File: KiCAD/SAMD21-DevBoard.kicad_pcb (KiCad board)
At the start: 2 copper layers, 28 x 60 mm, 34 parts, among them J1 .1" Headers, J2 .1" Headers, J3 Cortex_Debug, J4 USB-Micro, Q1 3.7A, 30V, SW1 B3FS-4005P, U1 SAMD21G18A-AU, U2 LM1117-5.0, U3 AP2112K-3.3, Y1 32.768KHz

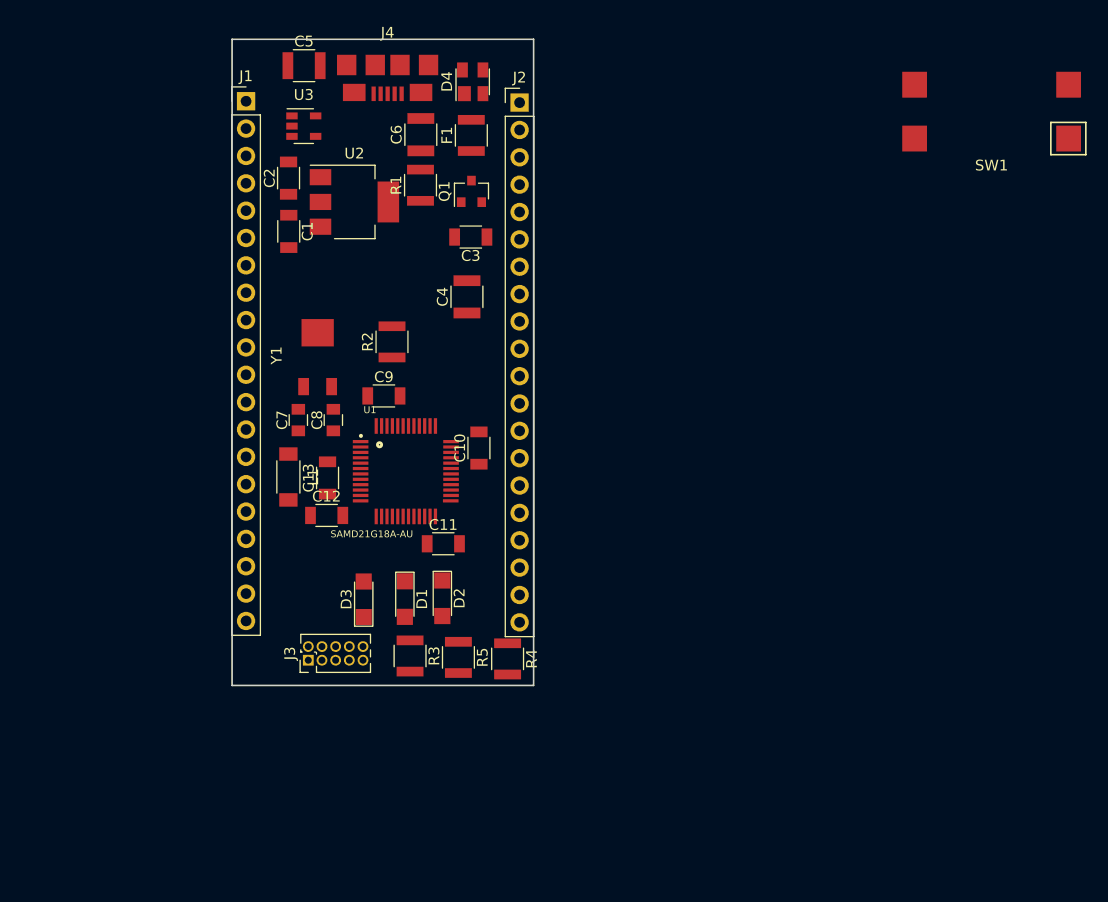
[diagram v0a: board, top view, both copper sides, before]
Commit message: Board layout and fixing schematic errors
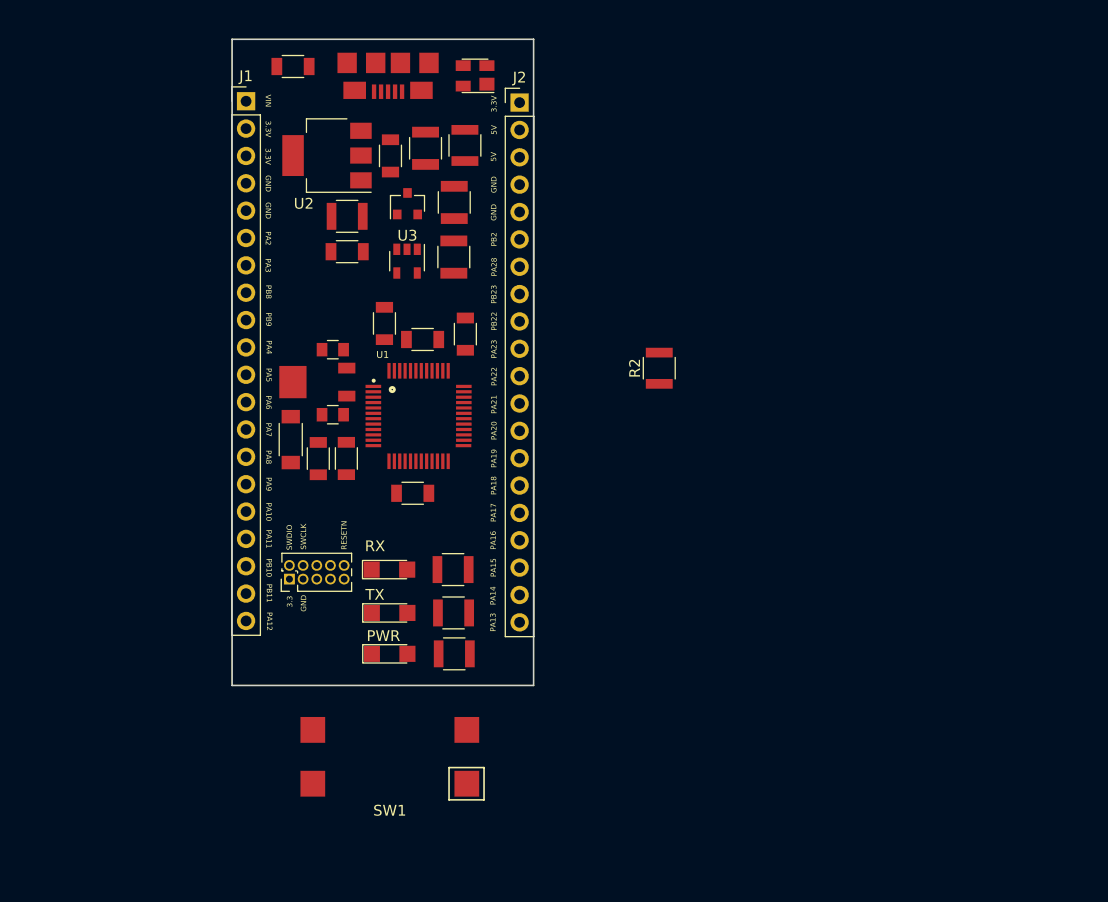
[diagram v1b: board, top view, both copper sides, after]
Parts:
- added C14: .1uF, Capacitors_SMD:C_1206, F.Cu at (157.7, 77.4)
- moved SW1 81.9 mm to (150.6, 116.6)
- moved R2 24.9 mm to (175.7, 80.5)
- moved C5 18.9 mm to (156.6, 65.2), turned to 270 degrees
- moved U3 15.8 mm to (152.2, 70.6), turned to 270 degrees
- moved C1 15.3 mm to (141.7, 52.5), turned to 0 degrees
- moved C10 14.5 mm to (150.1, 76.4)
- moved C3 11.6 mm to (146.7, 69.7), turned to 0 degrees
- moved C2 9.69 mm to (150.7, 60.8), turned to 270 degrees
- moved R3 8.96 mm to (156.5, 99.2), turned to 180 degrees
- moved J3 7.73 mm to (141.3, 100.1)
- moved R1 7.40 mm to (146.7, 66.4), turned to 180 degrees
- moved R4 6.59 mm to (156.6, 103.3), turned to 180 degrees
- moved C8 6.54 mm to (145.4, 78.8), turned to 0 degrees
- moved C9 6.35 mm to (153.7, 77.9)
- moved Q1 6.05 mm to (152.3, 65.3)
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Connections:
- C1 pad 2: +3V3 -> GND
- C10 pad 2: +3V3 -> GND
- C11 pad 2: +3V3 -> GND
- C12 pad 2: +3V3 -> GND
- C13 pad 2: +3V3 -> GND
- C2 pad 2: +3V3 -> GND
- C3 pad 2: +3V3 -> GND
- C4 pad 2: +3V3 -> GND
- C5 pad 2: +3V3 -> GND
- C6 pad 2: +3V3 -> GND
- C7 pad 1: +3V3 -> GND
- C8 pad 1: +3V3 -> GND
- C9 pad 2: +3V3 -> GND
- D3 pad 1: +3V3 -> GND
- D4 pad 1: +3V3 -> GND
- J1 pad 4: +3V3 -> GND
- J1 pad 5: +3V3 -> GND
- J2 pad 4: +3V3 -> GND
- J2 pad 5: +3V3 -> GND
- J3 pad 3: +3V3 -> GND
- J3 pad 5: +3V3 -> GND
- J4 pad 1: +3V3 -> GND
- J4 pad 6: +3V3 -> GND
- Q1 pad 1: +3V3 -> GND
- R1 pad 1: +3V3 -> GND
- SW1 pad 3: +3V3 -> GND
- SW1 pad 4: +3V3 -> GND
- U1 pad 18: +3V3 -> GND
- U1 pad 35: +3V3 -> GND
- U1 pad 42: +3V3 -> GND
- U1 pad 5: +3V3 -> GND
- U2 pad 1: +3V3 -> GND
- U3 pad 2: +3V3 -> GND
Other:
- board text added: "3.3"
- board text added: "3.3V"
- board text added: "5V"
- board text added: "GND"
- board text added: "PA10"
- board text added: "PA11"
- board text added: "PA12"
- board text added: "PA13"
- board text added: "PA14"
- board text added: "PA15"
- board text added: "PA16"
- board text added: "PA17"
- board text added: "PA18"
- board text added: "PA19"
- board text added: "PA2"
- board text added: "PA20"
- board text added: "PA21"
- board text added: "PA22"
- board text added: "PA23"
- board text added: "PA28"
- board text added: "PA3"
- board text added: "PA4"
- board text added: "PA5"
- board text added: "PA6"
- board text added: "PA7"
- board text added: "PA8"
- board text added: "PA9"
- board text added: "PB10"
- board text added: "PB11"
- board text added: "PB2"
- board text added: "PB22"
- board text added: "PB23"
- board text added: "PB8"
- board text added: "PB9"
- board text added: "PWR"
- board text added: "RESETN"
- board text added: "RX"
- board text added: "SWCLK"
- board text added: "SWDIO"
- board text added: "TX"
- board text added: "VIN"

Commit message: Place and route
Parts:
- U2: value LM1117-5.0 -> LM1117
- moved R2 29.5 mm to (147.0, 73.8), turned to 270 degrees
- moved J3 28.4 mm to (141.7, 71.8), turned to 0 degrees
- moved C9 2.37 mm to (153.8, 75.5)
- moved C1 1.92 mm to (142.3, 54.3), turned to 90 degrees
- moved C11 0.59 mm to (152.8, 92.8)
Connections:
- R3 pad 1: +5V -> +3V3
- R4 pad 1: +5V -> +3V3
- R5 pad 1: +5V -> +3V3
- U2 pad 4: (no net) -> +5V
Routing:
- net PA12: track 0.00 -> 55.6 mm, vias 0 -> 1
- net PB11: track 0.00 -> 42.5 mm, vias 0 -> 1
- net +5V: track 0.00 -> 39.7 mm, vias 0 -> 2
- net +3V3: track 0.00 -> 35.4 mm, vias 0 -> 11
- net PB10: track 0.00 -> 34.2 mm, vias 0 -> 3
- net GND: track 0.00 -> 24.2 mm
- net PA13: track 0.00 -> 22.2 mm
- net SWDIO: track 0.00 -> 21.1 mm, vias 0 -> 2
- net PA10: track 0.00 -> 19.5 mm, vias 0 -> 2
- net PA11: track 0.00 -> 18.7 mm, vias 0 -> 2
- net PA8: track 0.00 -> 17.0 mm
- net PA9: track 0.00 -> 16.6 mm
- net PA14: track 0.00 -> 16.6 mm
- net USB_D-: track 0.00 -> 16.5 mm, vias 0 -> 2
- net PA15: track 0.00 -> 15.4 mm
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- added copper zone on B.Cu, net +3V3
- added copper zone on F.Cu, net GND
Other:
- board text added: "Debug"
- board text removed: "3.3"
- board text removed: "RESETN"
- board text removed: "SWCLK"
- board text removed: "SWDIO"

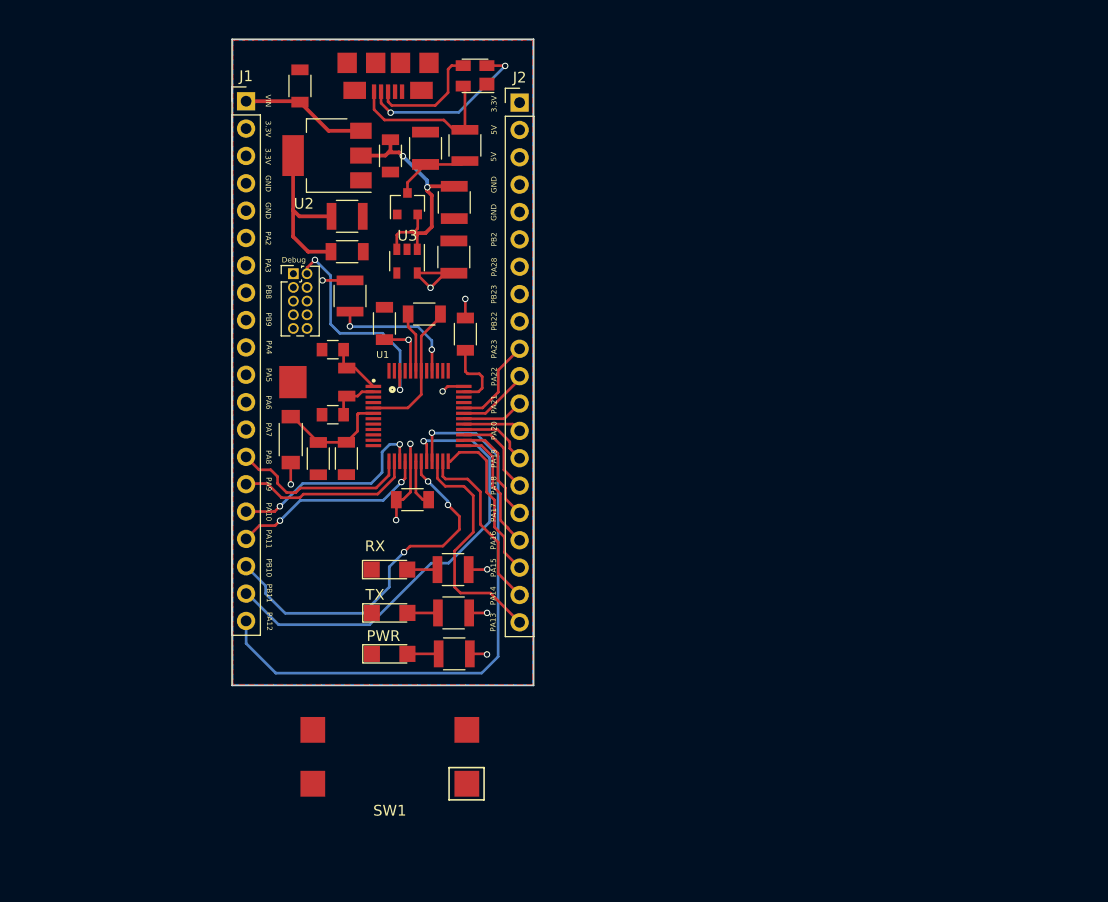
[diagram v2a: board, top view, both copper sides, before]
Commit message: Revising layout with different board outline
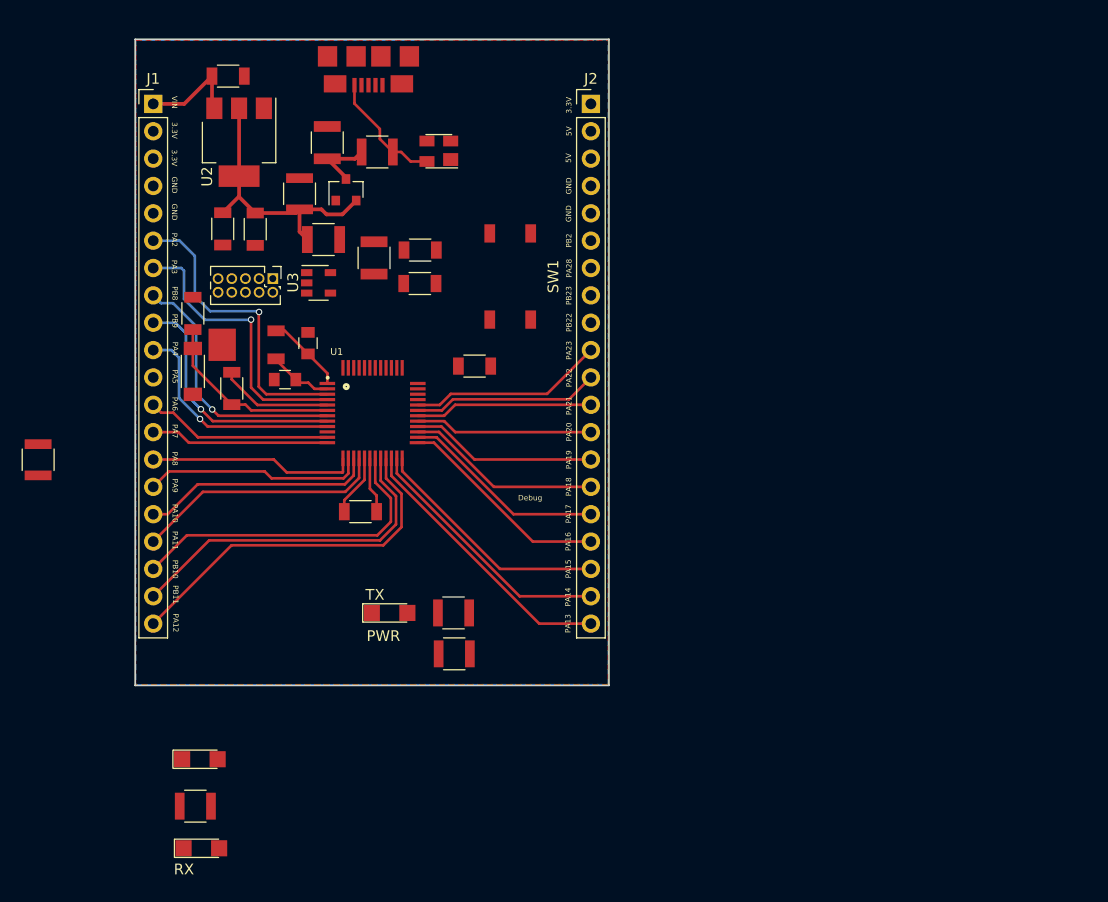
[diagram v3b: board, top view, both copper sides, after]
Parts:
- SW1: value B3FS-4005P -> FSMCTTR; footprint B3FS-4:B3FS-4 -> FSMCTTR:FSMCTTR
- moved SW1 46.0 mm to (161.8, 72.0), turned to 90 degrees
- moved R2 32.7 mm to (118.0, 89.0)
- moved R3 32.5 mm to (132.6, 121.2)
- moved D1 31.2 mm to (133.1, 125.1)
- moved D3 20.2 mm to (133.0, 116.9)
- moved C12 17.8 mm to (132.4, 75.5), turned to 90 degrees
- moved C2 17.0 mm to (135.1, 67.6)
- moved C5 12.6 mm to (144.5, 68.6), turned to 0 degrees
- moved C13 12.5 mm to (136.0, 82.4), turned to 90 degrees
- moved L1 11.1 mm to (132.4, 80.8)
- moved C6 9.14 mm to (144.8, 59.6)
- moved C3 8.79 mm to (138.2, 67.6), turned to 270 degrees
- moved J1 8.62 mm to (128.7, 56.0)
- moved U3 8.46 mm to (144.0, 72.6), turned to 0 degrees
- moved U2 8.26 mm to (136.7, 59.6), turned to 270 degrees
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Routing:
- net +3V3: track 35.4 -> 5.73 mm, vias 11 -> 0
- net PA2: track 0.00 -> 28.4 mm, vias 0 -> 1
- net PA3: track 0.00 -> 26.5 mm, vias 0 -> 1
- net PB8: track 0.00 -> 24.4 mm, vias 0 -> 1
- net PB9: track 0.00 -> 23.3 mm, vias 0 -> 1
- net PA12: track 55.6 -> 33.7 mm, vias 1 -> 0
- net PA4: track 0.00 -> 21.3 mm, vias 0 -> 1
- net SWDIO: track 21.1 -> 0.00 mm, vias 2 -> 0
- net PA6: track 0.00 -> 17.4 mm
- net PA7: track 0.00 -> 16.6 mm
- net USB_D-: track 16.5 -> 0.00 mm, vias 2 -> 0
- net +5V: track 39.7 -> 25.8 mm, vias 2 -> 0
- net RESETN: track 12.3 -> 0.00 mm, vias 2 -> 0
- net PA20: track 5.44 -> 16.5 mm
- net USB_D+: track 10.9 -> 0.00 mm
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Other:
- board size 28 x 60 mm -> 44 x 60 mm

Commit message: More routing
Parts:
- moved J3 35.3 mm to (158.4, 102.2)
- moved R2 26.0 mm to (138.2, 72.6), turned to 0 degrees
- moved D1 24.0 mm to (141.9, 102.8)
- moved R3 23.9 mm to (147.8, 102.8)
- moved D3 13.8 mm to (142.0, 106.3)
- moved D2 9.52 mm to (142.0, 99.3)
- moved R4 9.50 mm to (147.9, 99.3)
- moved R5 8.83 mm to (147.8, 106.3)
- moved C14 1.92 mm to (156.7, 79.7)
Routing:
- net GND: track 15.7 -> 154.1 mm, vias 0 -> 11
- net +3V3: track 5.73 -> 106.5 mm, vias 0 -> 9
- net RX_LED: track 0.00 -> 41.6 mm, vias 0 -> 4
- net RESETN: track 0.00 -> 34.0 mm, vias 0 -> 2
- net +5V: track 25.8 -> 58.5 mm
- net PB2: track 0.00 -> 30.6 mm
- net PA28: track 0.00 -> 24.5 mm
- net PB23: track 0.00 -> 22.3 mm
- net PB22: track 0.00 -> 19.9 mm
- net PA5: track 0.00 -> 19.3 mm
- net Net-(C9-Pad1): track 0.00 -> 9.14 mm, vias 0 -> 2
- net Net-(D2-Pad2): track 0.00 -> 2.85 mm
- net Net-(D1-Pad2): track 0.00 -> 2.78 mm
- net Net-(D3-Pad2): track 0.00 -> 2.77 mm
- net Net-(C7-Pad2): track 5.98 -> 6.71 mm

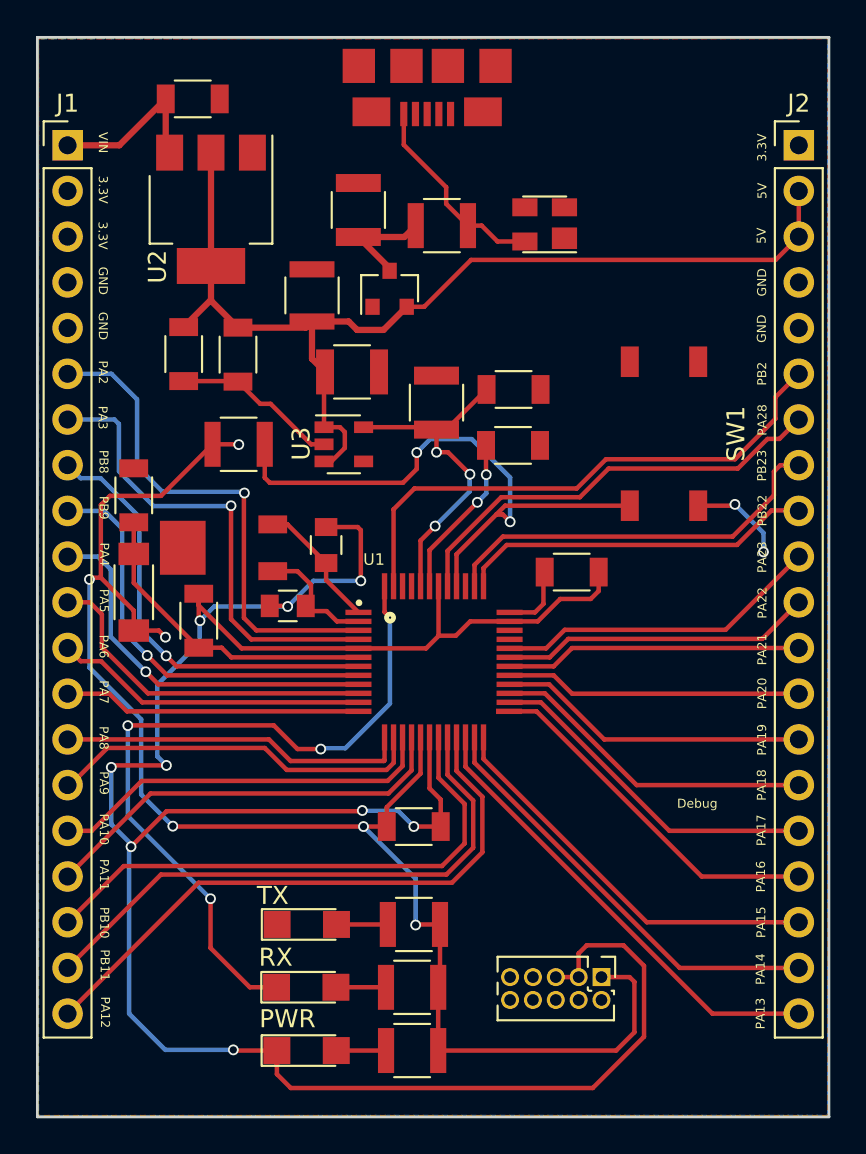
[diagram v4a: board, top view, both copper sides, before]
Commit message: Finished routing, now fine tweaking and tuning
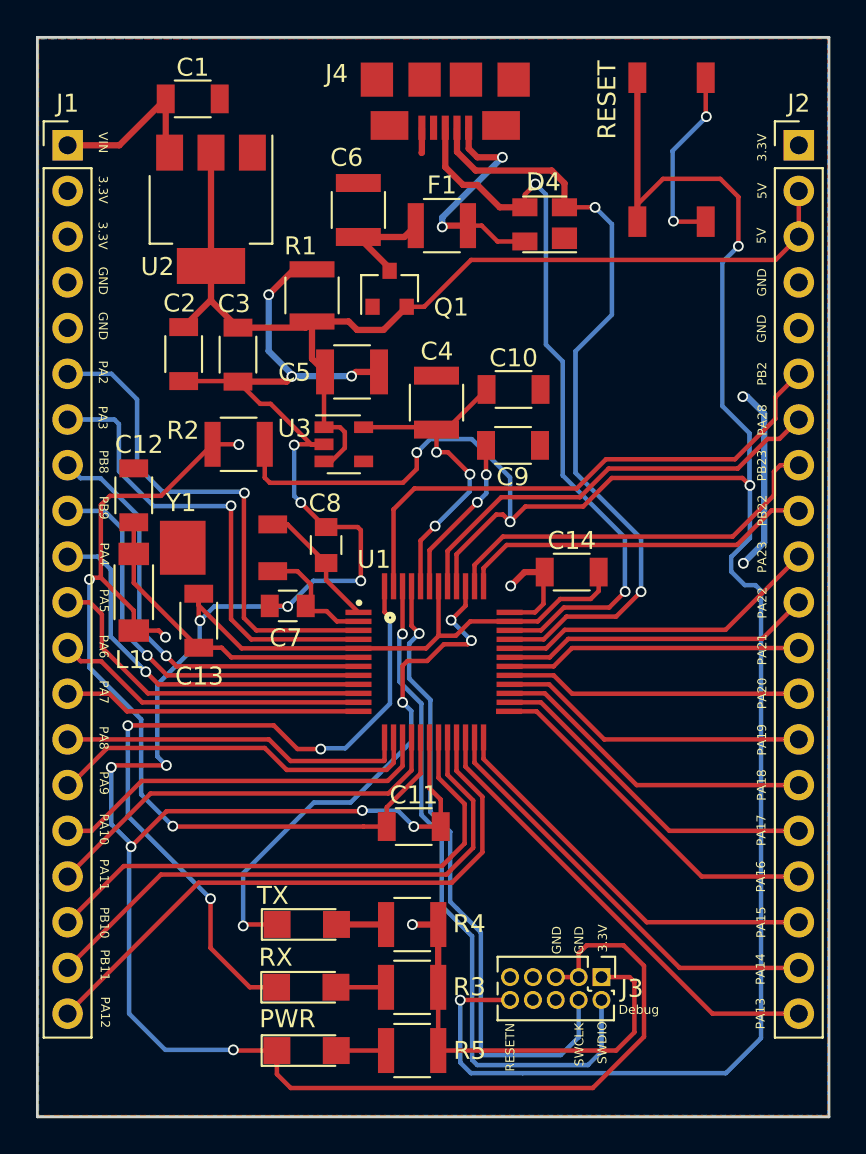
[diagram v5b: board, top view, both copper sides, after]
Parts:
- moved SW1 15.8 mm to (162.2, 56.2)
- moved J4 1.26 mm to (149.7, 52.3)
- moved R4 0.10 mm to (147.8, 99.3)
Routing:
- net RESETN: track 34.0 -> 129.6 mm, vias 2 -> 5
- net USB_D-: track 0.00 -> 43.6 mm, vias 0 -> 2
- net USB_D+: track 0.00 -> 41.1 mm, vias 0 -> 2
- net SWDIO: track 0.00 -> 38.6 mm, vias 0 -> 1
- net SWCLK: track 0.00 -> 35.9 mm, vias 0 -> 1
- net TX_LED: track 0.00 -> 29.9 mm, vias 0 -> 4
- net GND: track 154.1 -> 183.9 mm, vias 11 -> 16
- net (no net): track 0.00 -> 10.4 mm, vias 0 -> 2
- net +3V3: track 106.5 -> 102.2 mm
- net VBUS: track 11.2 -> 13.5 mm, vias 0 -> 2
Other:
- board text added: "RESET"
- board text added: "RESETN"
- board text added: "SAMD21 Dev Board Rev 0 UConn Formula SAE M. Cox - December 2018"
- board text added: "SWCLK"
- board text added: "SWDIO"
